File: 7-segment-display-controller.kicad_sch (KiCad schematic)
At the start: 49 parts, among them J101 Tag Connector, J102 USB_B_Micro, J103 JST 2.54 Header, J104 JST 2.54 Header, Q101 AO3501A, SW101 SW_DIP_x04, SW102 SW_Push, SW103 SW_Push, SW104 SW_Push, SW105 SW_Push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

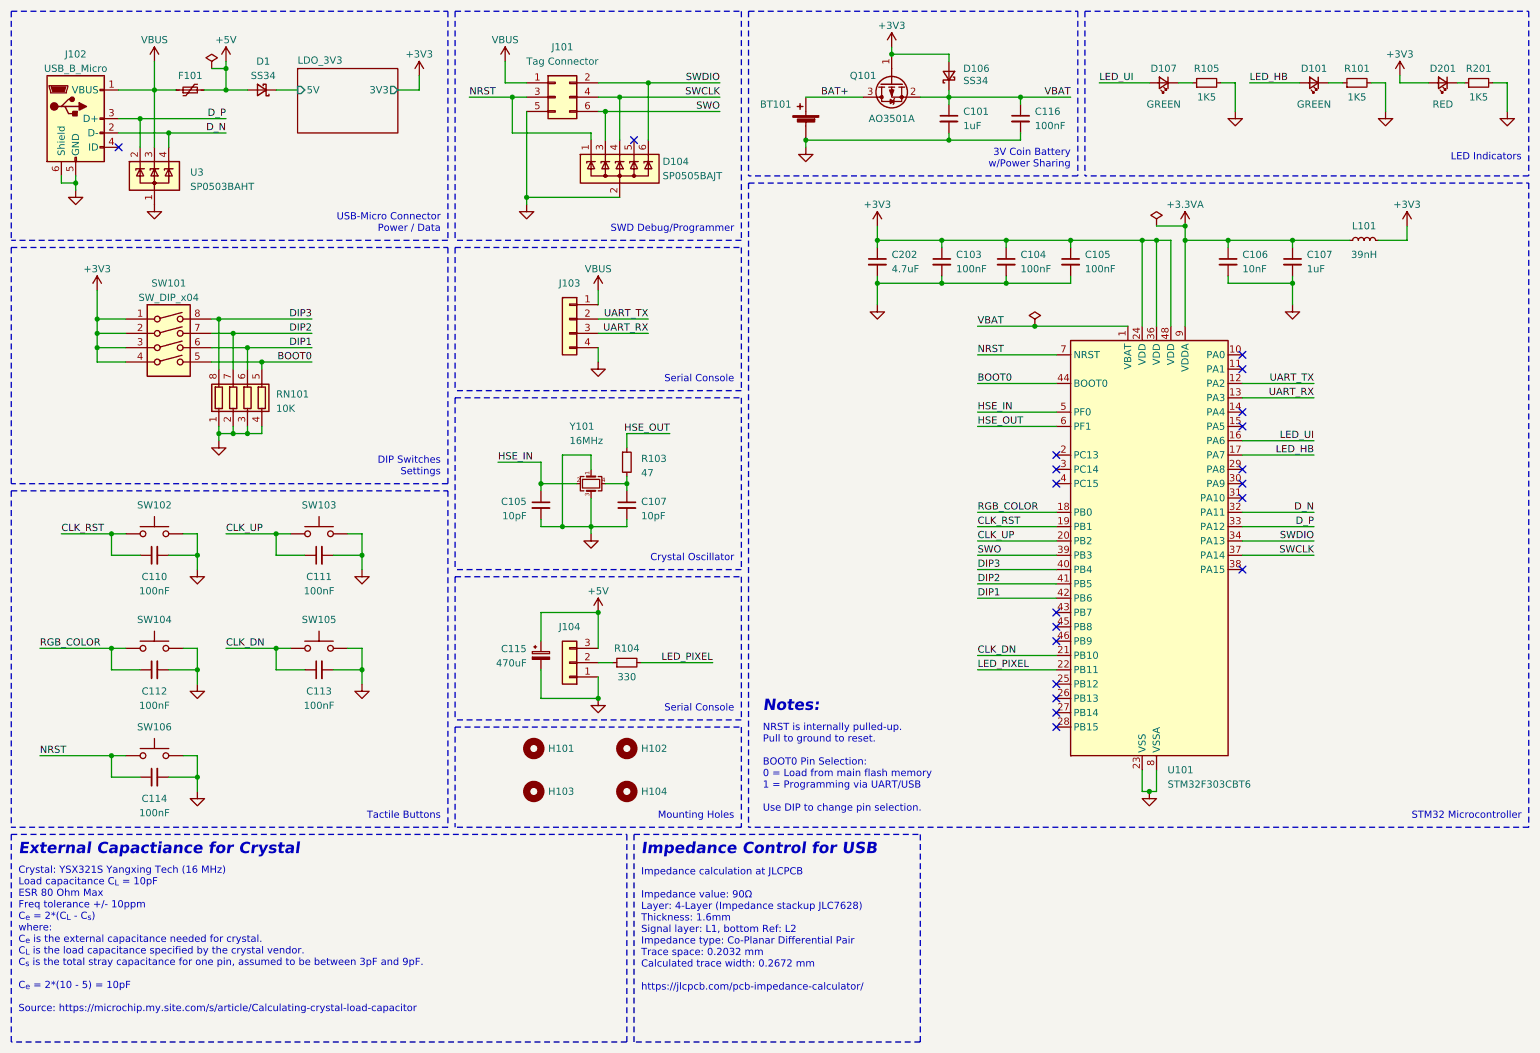
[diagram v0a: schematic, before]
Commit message: add alternate power source connector
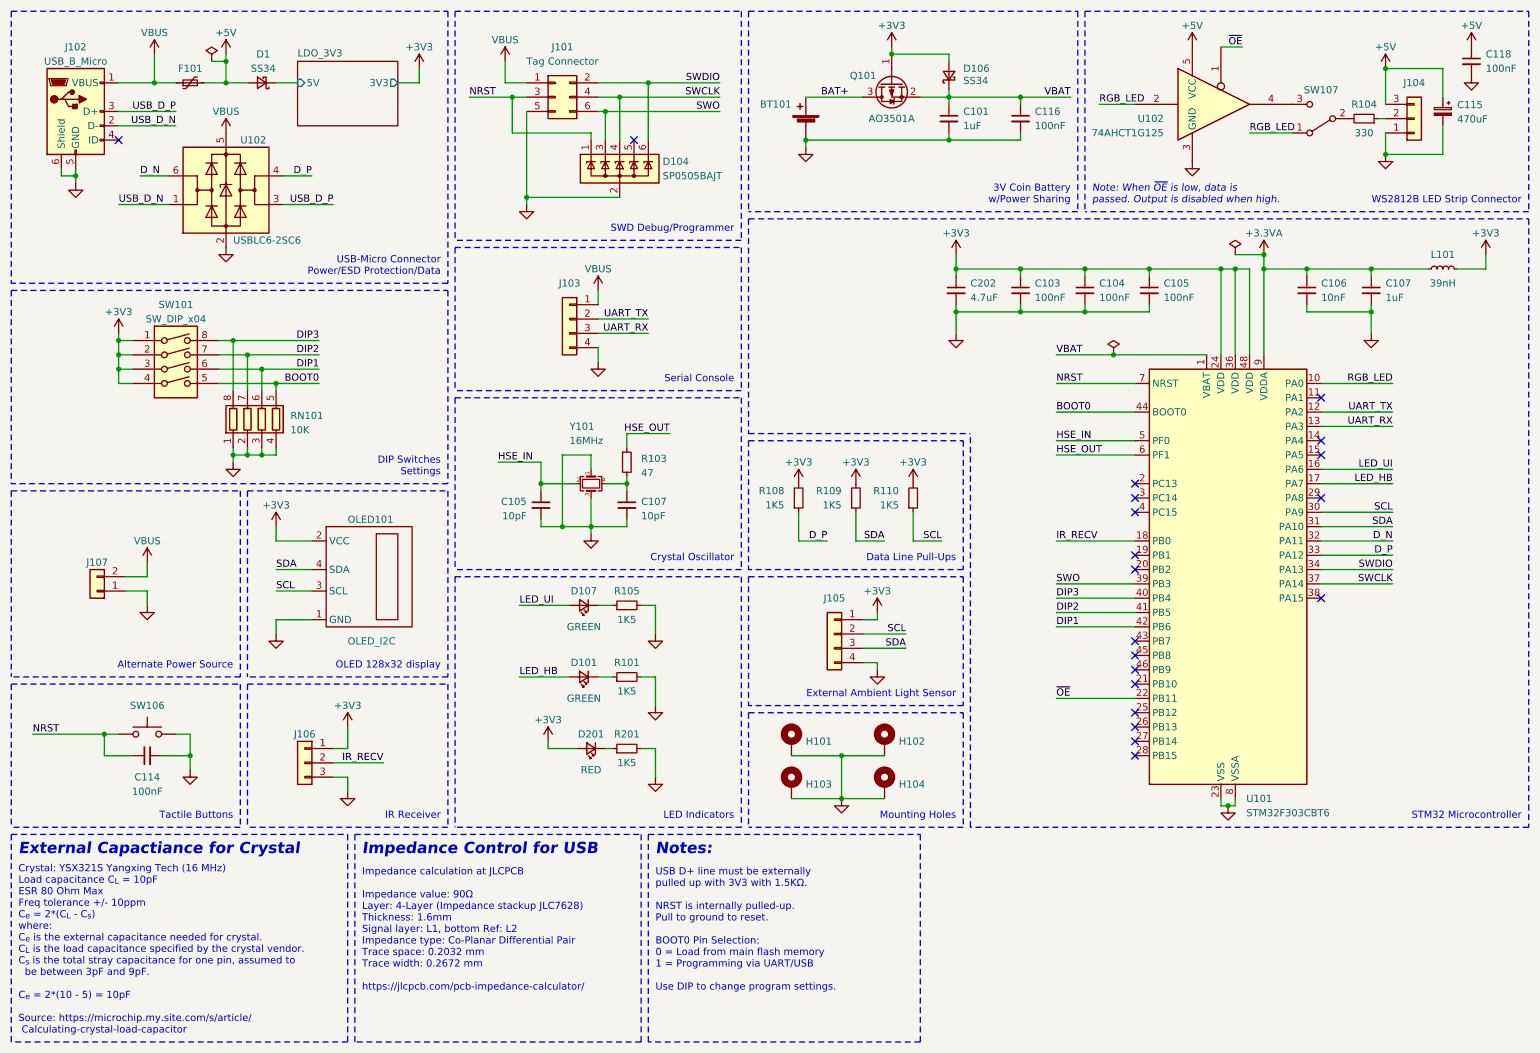
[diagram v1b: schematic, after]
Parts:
- removed C110, C111, C112, C113: 100nF, Capacitor_SMD:C_0603_1608Metric, symbol Device:C_Small
- removed SW102, SW103, SW104, SW105: SW_Push, Button_Switch_THT:SW_PUSH_6mm, symbol Switch:SW_Push
- removed U3: SP0503BAHT, User_Footprint:SOT-143-4, symbol Power_Protection:SP0503BAHT
- added C118: 100nF, Capacitor_SMD:C_0603_1608Metric, symbol Device:C_Small
- added J105: JST 2.54 Header, Connector_JST:JST_PH_B4B-PH-K_1x04_P2.00mm_Vertical, symbol Connector_Generic:Conn_01x04
- added J106: JST 2.54 Header, Connector_JST:JST_PH_B3B-PH-K_1x03_P2.00mm_Vertical, symbol Connector_Generic:Conn_01x03
- added J107: Conn_01x02, Connector_JST:JST_XH_B2B-XH-A_1x02_P2.50mm_Vertical, symbol Connector_Generic:Conn_01x02
- added OLED101: OLED_I2C, User_Footprint:OLED_128x32_I2C_4pins, symbol User Symbols:OLED_I2C
- added R108, R109, R110: 1K5, Resistor_SMD:R_0603_1608Metric, symbol Device:R_Small
- added SW107: SW_SPDT, Jumper:SolderJumper-3_P1.3mm_Open_RoundedPad1.0x1.5mm, symbol Switch:SW_SPDT
- added U102: USBLC6-2SC6, Package_TO_SOT_SMD:SOT-23-6, symbol Power_Protection:USBLC6-2SC6
- added U102: 74AHCT1G125, Package_TO_SOT_SMD:SOT-23-5, symbol 74xGxx:74AHCT1G125
- H101, H102, H103, H104: footprint MountingHole:MountingHole_4.3mm_M4_DIN965_Pad -> MountingHole:MountingHole_4.3mm_M4_Pad_Via; symbol Mechanical:MountingHole -> Mechanical:MountingHole_Pad
- J103: footprint Connector_JST:JST_XH_B4B-XH-A_1x04_P2.50mm_Vertical -> Connector_JST:JST_PH_B4B-PH-K_1x04_P2.00mm_Vertical
- R104: LCSC (none) -> C23138
- SW106: footprint Button_Switch_THT:SW_PUSH_6mm -> User_Footprint:XKB-Connectivity-TS-1187A-B-A-B; LCSC (none) -> C318884; now in the parts list
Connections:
- net +3V3: now also J105.1 (Pin_1), J106.1 (Pin_1), OLED101.2 (VCC), R108.2, R109.2, R110.2
- net +5V: now also C118.1, U102.5 (VCC)
- net D_N: now also U102.6 (I/O1); no longer J102.2 (D-)
- net D_P: now also R108.1, U102.4 (I/O2); no longer J102.3 (D+)
- net GND: now also H101.1, H102.1, H103.1, H104.1, C118.2, J105.4 (Pin_4), J106.3 (Pin_3), J107.1 (Pin_1), OLED101.1 (GND), U102.2 (GND), U102.3 (GND)
- net VBUS: now also J107.2 (Pin_2), U102.5 (VBUS)
- net RGB_LED: now reaches U101.10 (PA0)
- net RGB_LED: now also SW107.1 (A), U102.2
- net SCL: now reaches U101.30 (PA9)
- net SCL: now also J105.2 (Pin_2), OLED101.3 (SCL), R110.1
- net SDA: now reaches U101.31 (PA10)
- net SDA: now also J105.3 (Pin_3), OLED101.4 (SDA), R109.1
- net CLK_DN: no longer names the net of U101.21 (PB10)
- net CLK_RST: no longer names the net of U101.19 (PB1)
- net CLK_UP: no longer names the net of U101.20 (PB2)
- net LED_PIXEL: no longer names the net of R104.2
- net LED_PIXEL: now also SW107.2 (B); no longer U101.22 (PB11)
- net RGB_COLOR renamed IR_RECV
- net IR_RECV: now also J106.2 (Pin_2)
- new net: SW107.3 (C), U102.4
- new net USB_D_N: J102.2 (D-), U102.1 (I/O1)
- new net USB_D_P: J102.3 (D+), U102.3 (I/O2)
- new net ~{OE}: U101.22 (PB11), U102.1
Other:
- note added: "Alternate Power Source"
- note added: "Data Line Pull-Ups"
- note added: "External Ambient Light Sensor"
- note added: "IR Receiver"
- note added: "Impedance calculation at JLCPCB Impedance value: 90Ω Layer: 4-Layer (Impedance stackup JLC7628) Thickness: 1.6mm Signal layer: L1, bottom Ref: L2 Impedance type: Co-Planar Differential Pair Trace space: 0.2032 mm Trace width: 0.2672 mm https://jlcpcb.com/pcb-impedance-calculator/"
- note added: "Note: When ~{OE} is low, data is passed. Output is disabled when high."
- note added: "OLED 128x32 display"
- note added: "USB D+ line must be externally pulled up with 3V3 with 1.5KΩ. NRST is internally pulled-up. Pull to ground to reset. BOOT0 Pin Selection: 0 = Load from main flash memory 1 = Programming via UART/USB Use DIP to change program settings."
- note added: "USB-Micro Connector Power/ESD Protection/Data"
- note added: "WS2812B LED Strip Connector"
- note removed: "Impedance calculation at JLCPCB Impedance value: 90Ω Layer: 4-Layer (Impedance stackup JLC7628) Thickness: 1.6mm Signal layer: L1, bottom Ref: L2 Impedance type: Co-Planar Differential Pair Trace space: 0.2032 mm Calculated trace width: 0.2672 mm https://jlcpcb.com/pcb-impedance-calculator/"
- note removed: "NRST is internally pulled-up. Pull to ground to reset. BOOT0 Pin Selection: 0 = Load from main flash memory 1 = Programming via UART/USB Use DIP to change pin selection."
- note removed: "USB-Micro Connector Power / Data"
- moved on the sheet: C103, C104, C105, C106, C107, C114, C115, C202, D1, D101, D107, D201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

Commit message: add 32.768KHz crystal
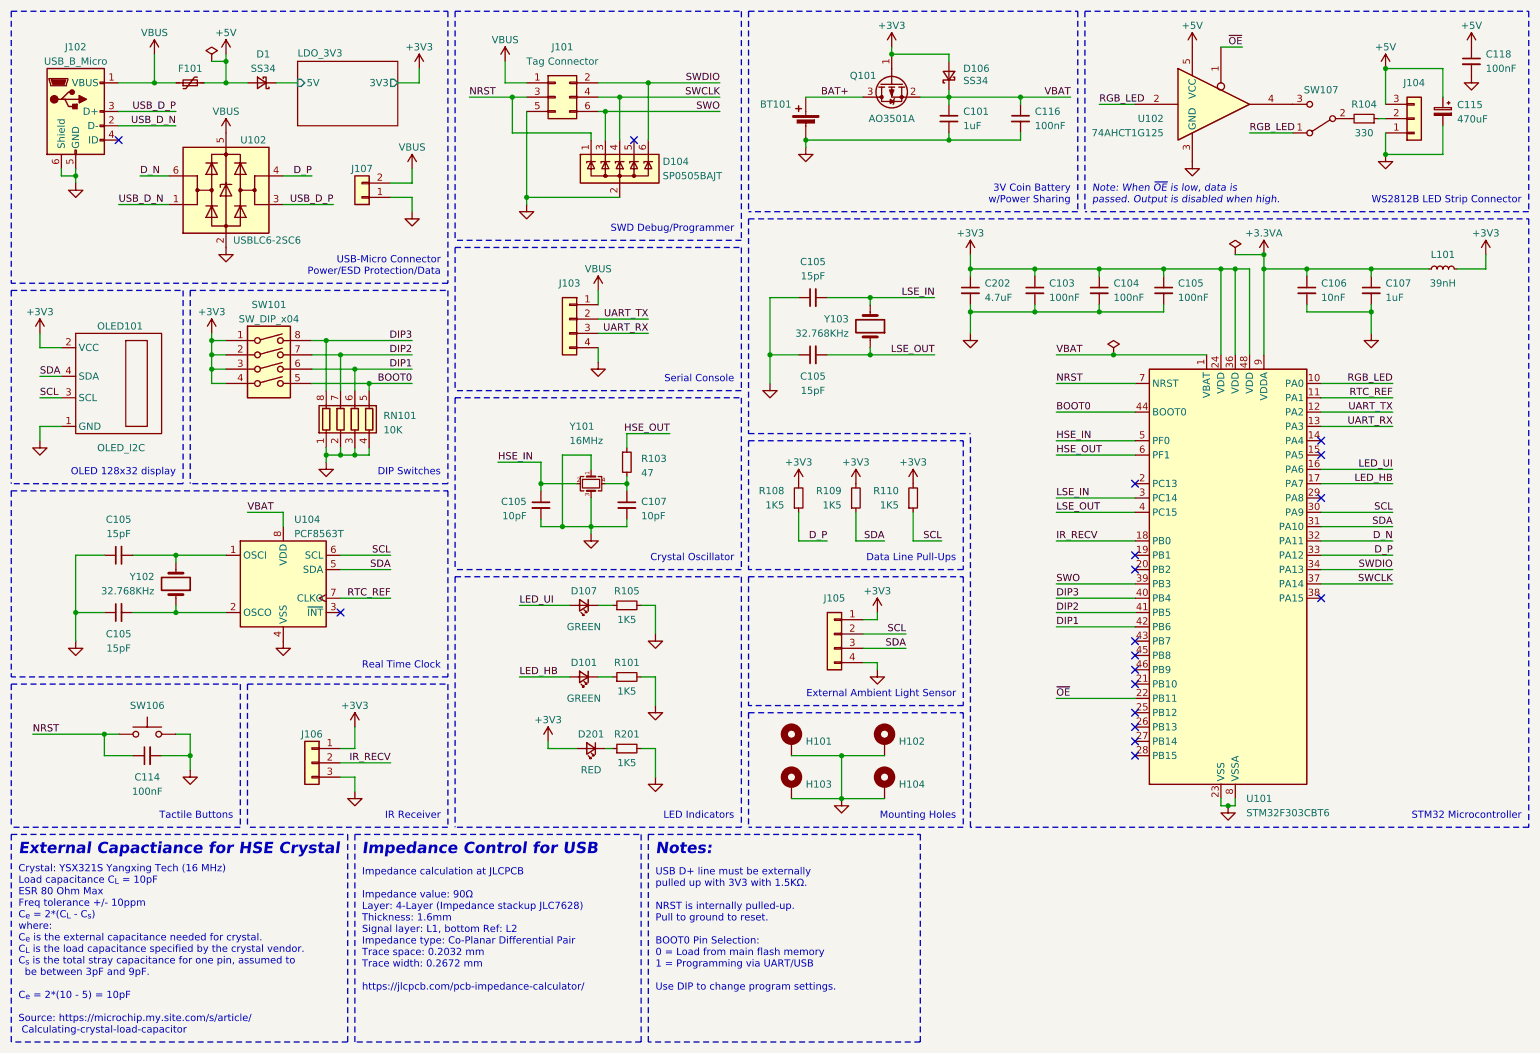
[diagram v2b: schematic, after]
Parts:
- added C105 (x4): 15pF, Capacitor_SMD:C_0603_1608Metric, symbol Device:C_Small
- added U104: PCF8563T, Package_SO:SOIC-8_3.9x4.9mm_P1.27mm, symbol Timer_RTC:PCF8563T
- added Y102, Y103: 32.768KHz, Crystal:Crystal_SMD_3215-2Pin_3.2x1.5mm, symbol Device:Crystal
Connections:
- net GND: now also C105.1, C105.1, C105.1, C105.1, U104.4 (VSS)
- net SCL: now also U104.6 (SCL)
- net SDA: now also U104.5 (SDA)
- net VBAT: now also U104.8 (VDD)
- net RTC_REF: now reaches U101.11 (PA1)
- net RTC_REF: now also U104.7 (CLKO)
- net LSE_IN: now reaches U101.3 (PC14)
- net LSE_IN: now also C105.2, Y103.2
- net LSE_OUT: now reaches U101.4 (PC15)
- net LSE_OUT: now also C105.2, Y103.1
- new net: C105.2, U104.2 (OSCO), Y102.1
- new net: C105.2, U104.1 (OSCI), Y102.2
- no-connect marks 20 -> 18
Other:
- note added: "DIP Switches"
- note added: "External Capactiance for HSE Crystal"
- note added: "Real Time Clock"
- note removed: "Alternate Power Source"
- note removed: "DIP Switches Settings"
- note removed: "External Capactiance for Crystal"
- moved on the sheet: C103, C104, C105, C202, J106, J107, OLED101, RN101, SW101

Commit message: fix crystal pin assignments
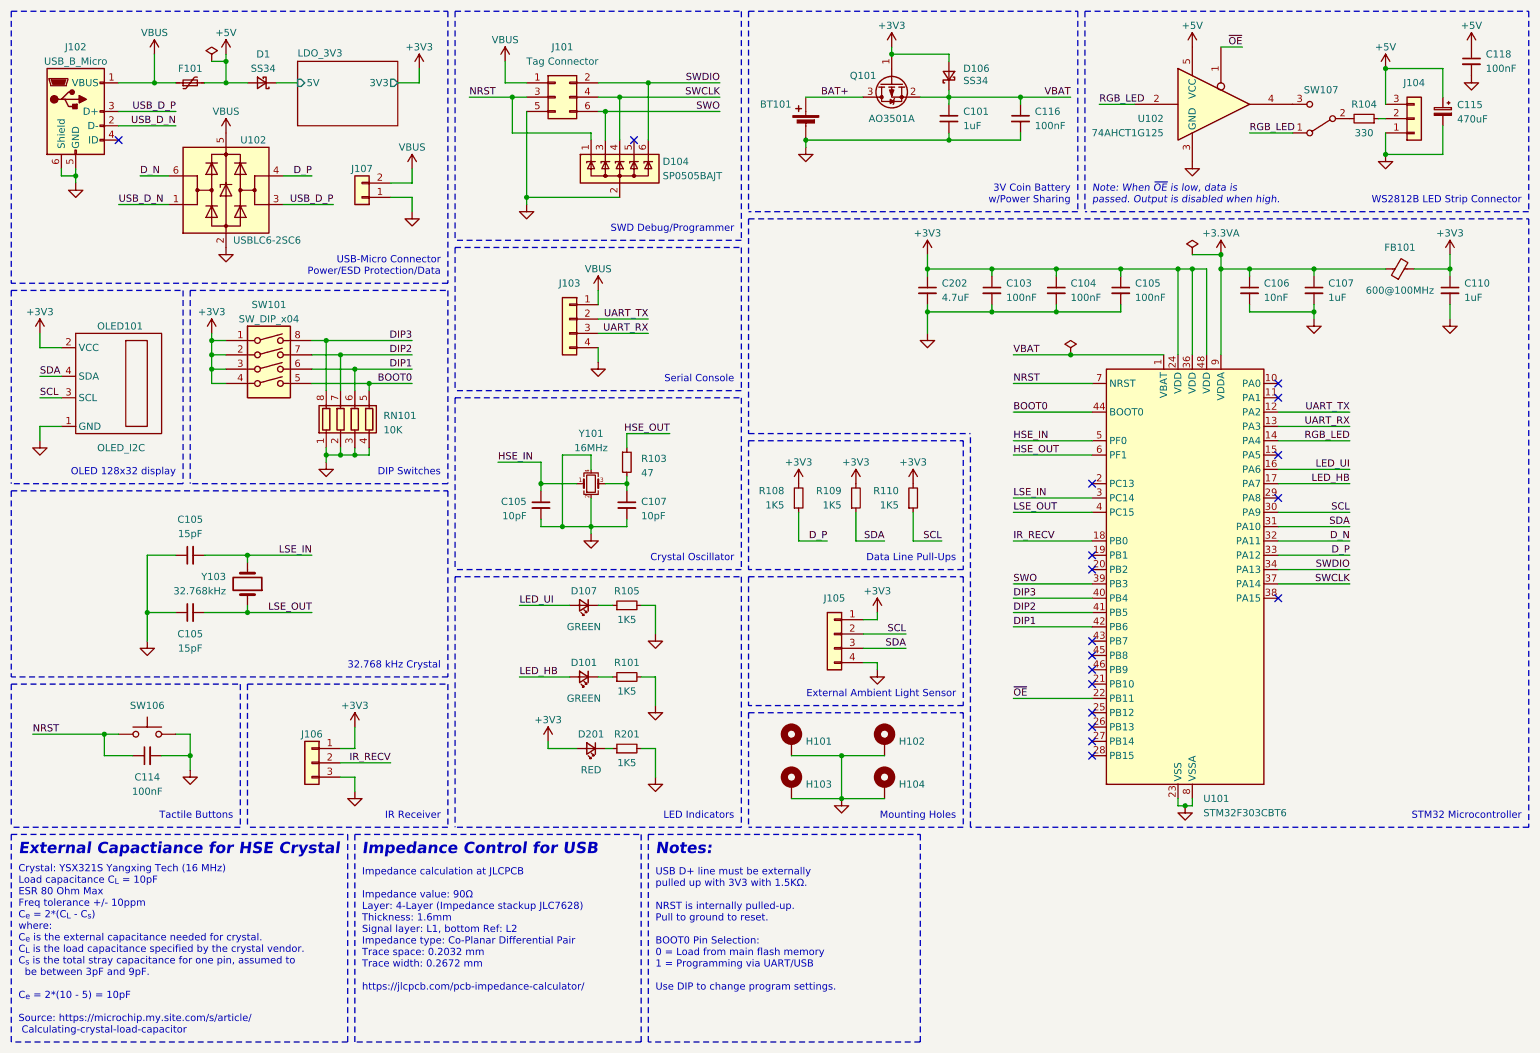
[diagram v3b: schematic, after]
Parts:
- removed C105 (x2): 15pF, Capacitor_SMD:C_0603_1608Metric, symbol Device:C_Small
- removed U104: PCF8563T, Package_SO:SOIC-8_3.9x4.9mm_P1.27mm, symbol Timer_RTC:PCF8563T
- removed Y102: 32.768KHz, Crystal:Crystal_SMD_3215-2Pin_3.2x1.5mm, symbol Device:Crystal
- added C110: 1uF, Capacitor_SMD:C_0603_1608Metric, symbol Device:C_Small
- C105: LCSC (none) -> C1644
- FB101: renamed from L101; value 39nH -> 600@100MHz; footprint Inductor_SMD:L_0402_1005Metric -> Inductor_SMD:L_0805_2012Metric_Pad1.15x1.40mm_HandSolder; symbol Device:L_Small -> Device:FerriteBead_Small; LCSC C26443 -> C1017
- H101, H102, H103, H104: footprint MountingHole:MountingHole_4.3mm_M4_Pad_Via -> MountingHole:MountingHole_3.2mm_M3_Pad_Via
- Y103: value 32.768KHz -> 32.768kHz; LCSC (none) -> C32346
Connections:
- net +3V3: now also C110.1
- net GND: now also Y101.2, Y101.4, C110.2; no longer Y101.1, Y101.3
- net HSE_IN: now also Y101.1; no longer Y101.2
- net RGB_LED: now also U101.14 (PA4); no longer U101.10 (PA0)
- net at C107.1, R103.2: now also Y101.3; no longer Y101.4
- net RTC_REF: no longer names the net of U101.11 (PA1)
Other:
- note added: "32.768 kHz Crystal"
- note removed: "Real Time Clock"
- moved on the sheet: C103, C104, C105, C106, C107, C202, U101, Y101, Y103
